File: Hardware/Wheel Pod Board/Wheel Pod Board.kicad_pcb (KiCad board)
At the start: 2 copper layers, 90 x 25.4 mm, 30 parts, among them J1 Conn_RJ-45, P1 UIM240XX_Stepper_Conn, P2 RS232, P3 ST_SWD_Connector, P4 SyRen, P5 BATT, U1 STM32F401RCT6, U2 SN75176BDR, U3 ZXCT1107, U4 ZXCT1107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

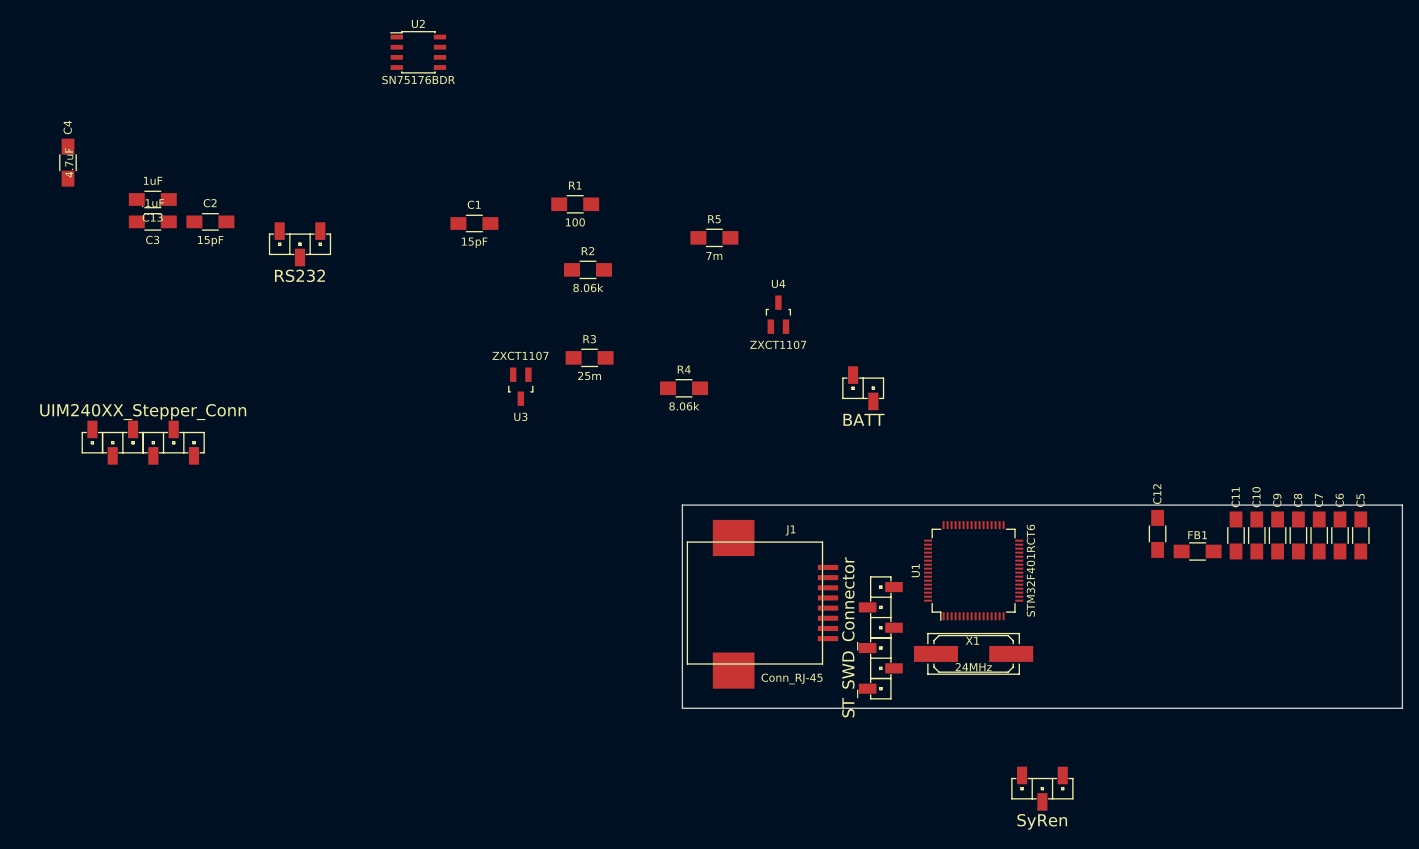
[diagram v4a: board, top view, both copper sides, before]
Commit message: Position components on PCB
Closes #4
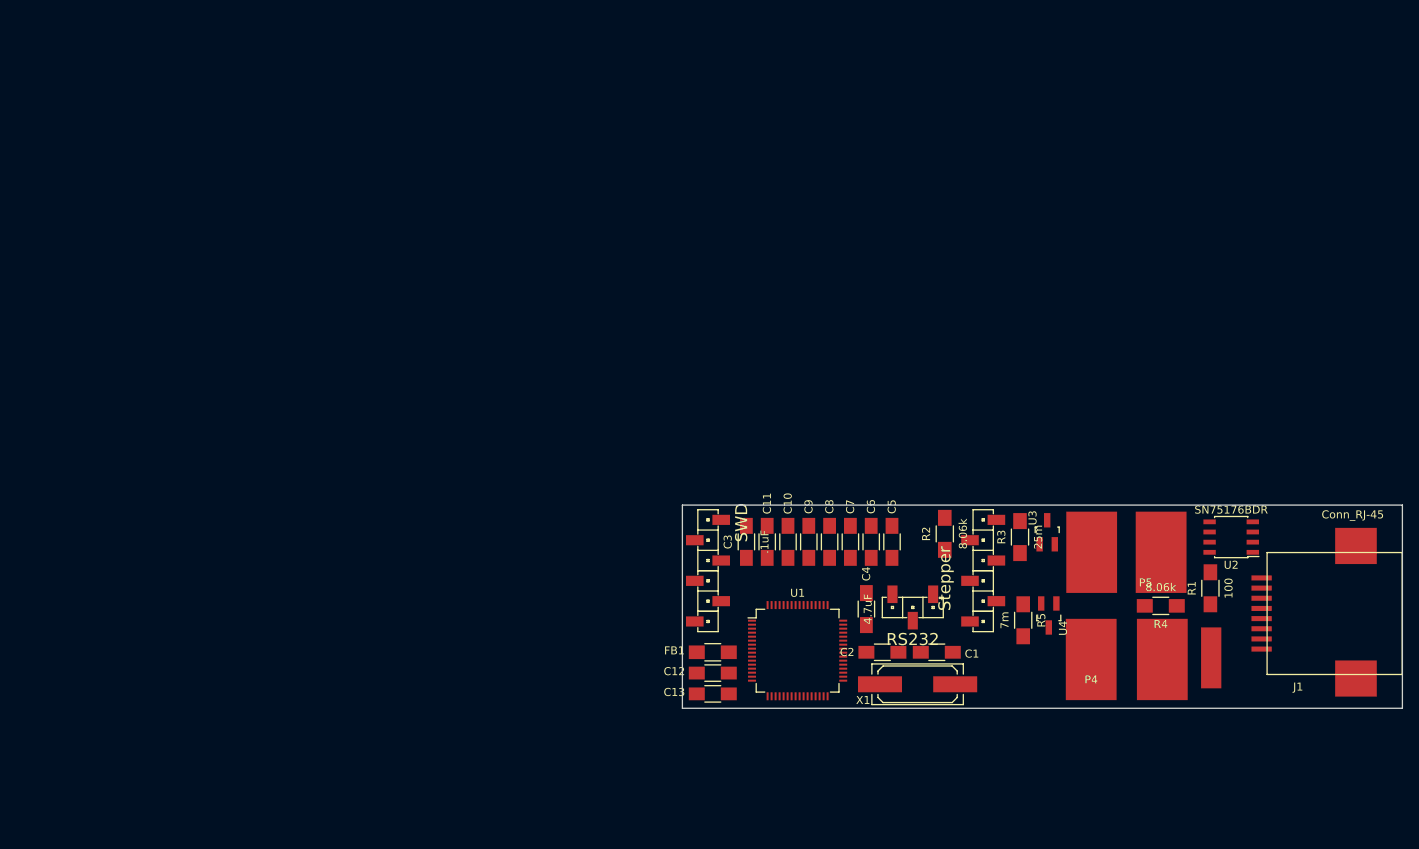
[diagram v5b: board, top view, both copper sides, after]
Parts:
- P1: value UIM240XX_Stepper_Conn -> Stepper
- P3: value ST_SWD_Connector -> SWD
- P4: footprint MAVRIC_footprints:1x3_SMD_header -> Wire_Pads:SolderWirePad_3x_0-8mmDrill
- P5: footprint MAVRIC_footprints:1x2_SMD_header -> Wire_Pads:SolderWirePad_2x_0-8mmDrill
- U3, U4: value ZXCT1107 -> (none)
- moved U2 118.3 mm to (262.0, 132.8), turned to 180 degrees
- moved C4 114.3 mm to (216.4, 141.8)
- moved P1 106.2 mm to (231.0, 137.0), turned to 270 degrees
- moved C2 99.8 mm to (218.4, 147.2)
- moved C13 93.4 mm to (197.2, 152.4)
- moved R1 92.8 mm to (259.4, 139.2), turned to 90 degrees
- moved P2 89.0 mm to (222.2, 141.6)
- moved C3 84.3 mm to (201.4, 133.4), turned to 90 degrees
- moved C1 78.8 mm to (225.2, 147.2), turned to 180 degrees
- moved U3 68.3 mm to (239.0, 132.2), turned to 0 degrees
- moved R4 65.5 mm to (253.2, 141.4), turned to 180 degrees
- moved FB1 61.9 mm to (197.2, 147.2), turned to 0 degrees
- moved R5 61.4 mm to (236.0, 143.2), turned to 270 degrees
- moved C11 58.6 mm to (204.0, 133.4)
- moved C6 58.6 mm to (217.0, 133.4)
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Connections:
- P1 pad 1: +12V -> /Stp+12V

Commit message: Begin routing PCB
Starting #8
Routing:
- net +3V3: track 0.00 -> 68.8 mm
- net GND: track 0.00 -> 44.0 mm, vias 0 -> 6
- net /VDDA: track 0.00 -> 5.73 mm
- added copper zone on B.Cu, net GND
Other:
- net class Default: clearance 0.254 -> 0.2032; trace_width 0.254 -> 0.2032
- rule trace_clearance: 0.254 -> 0.2032
- rule trace_min: 0.254 -> 0.2032
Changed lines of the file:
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@@
   (general
     (links 80)
-    (no_connects 80)
+    (no_connects 54)
     (area 193.349999 128.749999 283.450001 154.250001)
     (thickness 1.6)
     (drawings 4)
-    (tracks 0)
+    (tracks 52)
     (zones 0)
     (modules 30)
@@
   )
   (setup
-    (last_trace_width 0.254)
-    (trace_clearance 0.254)
-    (zone_clearance 0.508)
+    (last_trace_width 0.2032)
+    (user_trace_width 2.032)
+    (trace_clearance 0.2032)
+    (zone_clearance 0.1778)
     (zone_45_only no)
-    (trace_min 0.254)
+    (trace_min 0.2032)
     (segment_width 0.2)
     (edge_width 0.1)
@@
   (net 66 /USART2_TX)
   (net_class Default "This is the default net class."
-    (clearance 0.254)
-    (trace_width 0.254)
+    (clearance 0.2032)
+    (trace_width 0.2032)
     (via_dia 0.889)
     (via_drill 0.635)
@@
   (gr_line (start 193.4 154.2) (end 283.4 154.2) (angle 90) (layer Edge.Cuts) (width 0.1))
   (gr_line (start 193.4 128.8) (end 193.4 154.2) (angle 90) (layer Edge.Cuts) (width 0.1))
+  (segment (start 228.2 131.5) (end 228.2 132.04) (width 0.2032) (layer F.Cu) (net 40))
+  (via (at 228.2 131.5) (size 0.889) (layers F.Cu B.Cu) (net 40))
+  (segment (start 226.2 133.5) (end 228.2 131.5) (width 0.2032) (layer F.Cu) (net 40) (status 400000))
+  (segment (start 228.2 132.04) (end 229.35 133.19) (width 0.2032) (layer F.Cu) (net 40) (status 800000))
+  (segment (start 226.2 134.4) (end 226.2 133.5) (width 0.2032) (layer F.Cu) (net 40) (status C00000))
+  (segment (start 219.6 131.4) (end 220.8 131.4) (width 0.2032) (layer F.Cu) (net 40) (status 400000))
+  (via (at 221.5 130.7) (size 0.889) (layers F.Cu B.Cu) (net 40))
+  (segment (start 220.8 131.4) (end 221.5 130.7) (width 0.2032) (layer F.Cu) (net 40))
+  (segment (start 217 131.4) (end 219.6 131.4) (width 0.2032) (layer F.Cu) (net 40) (status C00000))
+  (segment (start 199.1 133) (end 199.8 133) (width 0.2032) (layer F.Cu) (net 40))
+  (segment (start 198.25 133.85) (end 199.1 133) (width 0.2032) (layer F.Cu) (net 40))
+  (via (at 199.1 133) (size 0.889) (layers F.Cu B.Cu) (net 40))
+  (segment (start 198.25 135.73) (end 198.25 133.85) (width 0.2032) (layer F.Cu) (net 40) (status 400000))
+  (segment (start 199.8 133) (end 201.4 131.4) (width 0.2032) (layer F.Cu) (net 40) (status 800000))
+  (segment (start 201.4 131.4) (end 206.6 131.4) (width 0.2032) (layer F.Cu) (net 40) (status C00000))
+  (segment (start 206.6 131.4) (end 209.2 131.4) (width 0.2032) (layer F.Cu) (net 40) (status C00000))
+  (segment (start 209.2 131.4) (end 211.8 131.4) (width 0.2032) (layer F.Cu) (net 40) (status C00000))
+  (segment (start 211.8 131.4) (end 214.4 131.4) (width 0.2032) (layer F.Cu) (net 40) (status C00000))
+  (segment (start 214.4 131.4) (end 217 131.4) (width 0.2032) (layer F.Cu) (net 40) (status C00000))
+  (segment (start 195.2 152.4) (end 195.2 149.8) (width 0.2032) (layer F.Cu) (net 40) (status C00000))
+  (segment (start 195.2 149.8) (end 195.6 149.4) (width 0.2032) (layer F.Cu) (net 40) (status C00000))
+  (segment (start 195.6 149.4) (end 197.1 149.4) (width 0.2032) (layer F.Cu) (net 40) (status 400000))
+  (via (at 197.1 149.4) (size 0.889) (layers F.Cu B.Cu) (net 40))
+  (segment (start 202.1 148.75) (end 203.15 148.75) (width 0.2032) (layer F.Cu) (net 40) (status 400000))
+  (segment (start 204.55 150.15) (end 204.55 152.7) (width 0.2032) (layer F.Cu) (net 40))
+  (via (at 204 149.6) (size 0.889) (layers F.Cu B.Cu) (net 40))
+  (segment (start 204.55 150.15) (end 204 149.6) (width 0.2032) (layer F.Cu) (net 40))
+  (segment (start 203.15 148.75) (end 204 149.6) (width 0.2032) (layer F.Cu) (net 40))
+  (segment (start 211.05 152.7) (end 211.05 151.65) (width 0.2032) (layer F.Cu) (net 40))
+  (via (at 210.8 151.4) (size 0.889) (layers F.Cu B.Cu) (net 40))
+  (segment (start 211.05 151.65) (end 210.8 151.4) (width 0.2032) (layer F.Cu) (net 40))
+  (segment (start 195.2 147.2) (end 196.4 147.2) (width 0.2032) (layer F.Cu) (net 44) (status 400000))
+  (segment (start 196.4 147.2) (end 204.05 139.55) (width 0.2032) (layer F.Cu) (net 44))
+  (segment (start 211.55 152.7) (end 211.55 144.35) (width 0.2032) (layer F.Cu) (net 44))
+  (segment (start 211.55 144.35) (end 210.45 143.25) (width 0.2032) (layer F.Cu) (net 44))
+  (segment (start 205.05 152.7) (end 205.05 145.05) (width 0.2032) (layer F.Cu) (net 44))
+  (segment (start 203.25 143.25) (end 202.1 143.25) (width 0.2032) (layer F.Cu) (net 44))
+  (segment (start 205.05 145.05) (end 203.25 143.25) (width 0.2032) (layer F.Cu) (net 44))
+  (segment (start 202.1 143.25) (end 210.45 143.25) (width 0.2032) (layer F.Cu) (net 44))
+  (segment (start 210.45 143.25) (end 213.5 143.25) (width 0.2032) (layer F.Cu) (net 44))
+  (segment (start 204.05 141.3) (end 202.1 143.25) (width 0.2032) (layer F.Cu) (net 44))
+  (segment (start 204.05 141.3) (end 204.05 139.55) (width 0.2032) (layer F.Cu) (net 44))
+  (segment (start 204.05 139.55) (end 204.05 135.45) (width 0.2032) (layer F.Cu) (net 44))
+  (segment (start 204.05 135.45) (end 204.1 135.4) (width 0.2032) (layer F.Cu) (net 44))
+  (segment (start 204.1 135.4) (end 209.2 135.4) (width 0.2032) (layer F.Cu) (net 44))
+  (segment (start 209.2 135.4) (end 211.8 135.4) (width 0.2032) (layer F.Cu) (net 44))
+  (segment (start 211.8 135.4) (end 214.4 135.4) (width 0.2032) (layer F.Cu) (net 44))
+  (segment (start 214.4 135.4) (end 217 135.4) (width 0.2032) (layer F.Cu) (net 44))
+  (segment (start 217 135.4) (end 219.6 135.4) (width 0.2032) (layer F.Cu) (net 44))
+  (segment (start 199.2 147.2) (end 199.2 149.8) (width 0.2032) (layer F.Cu) (net 45) (status C00000))
+  (segment (start 199.2 149.8) (end 199.75 149.25) (width 0.2032) (layer F.Cu) (net 45) (status C00000))
+  (segment (start 199.75 149.25) (end 202.1 149.25) (width 0.2032) (layer F.Cu) (net 45) (status C00000))
+  (zone (net 40) (net_name GND) (layer B.Cu) (hatch edge 0.508)
+    (connect_pads (clearance 0.1778))
+    (min_thickness 0.1778)
+    (fill yes (arc_segments 16) (thermal_gap 0.508) (thermal_bridge_width 0.508))
+    (polygon
+      (pts
+        (xy 283.2 154) (xy 193.6 154) (xy 193.6 129) (xy 283.2 129)
+      )
+    )
+  )
 )

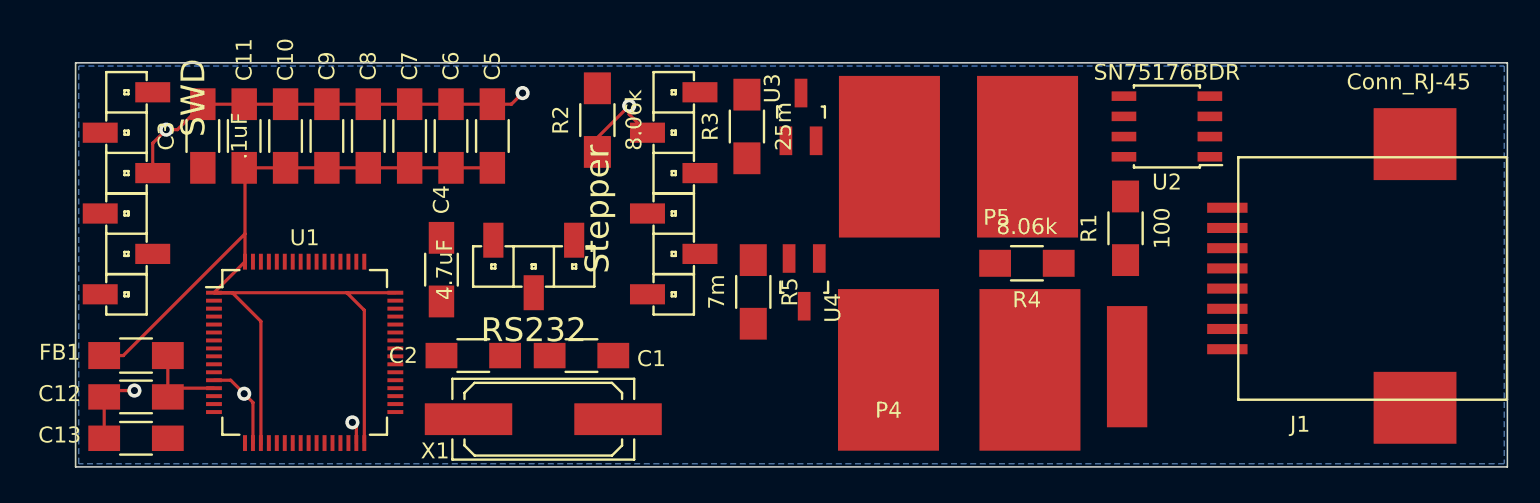
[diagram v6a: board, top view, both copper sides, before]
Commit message: Route all components, generate export + images
Progressing #8, Close #9 for now
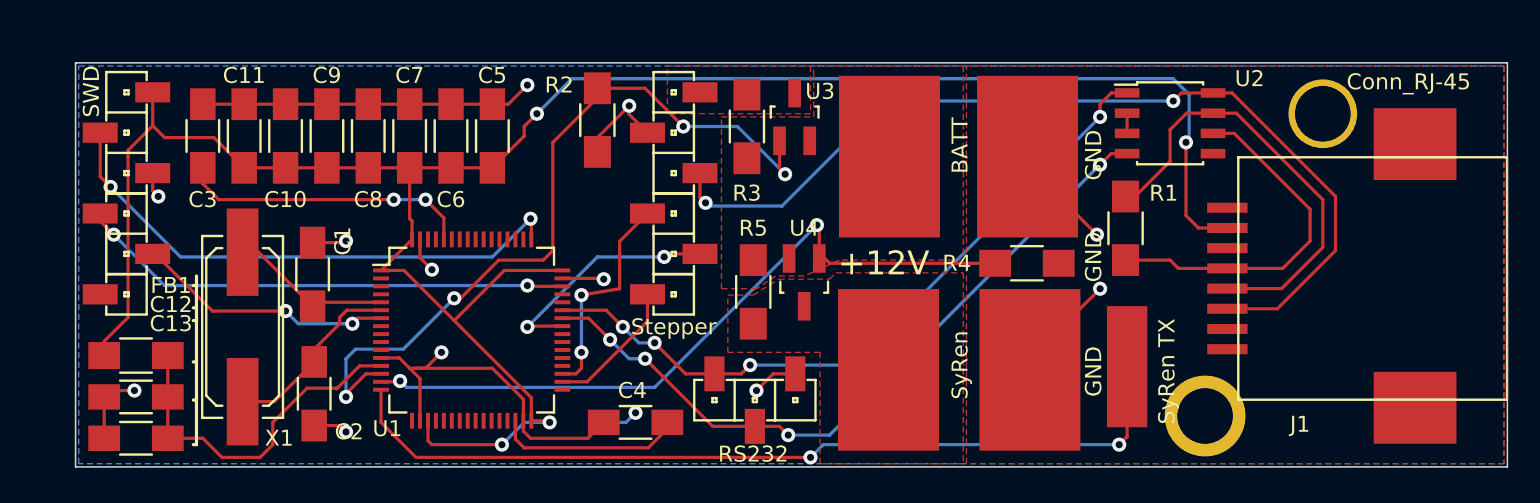
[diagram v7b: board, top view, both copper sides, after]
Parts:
- added MountingHole_3-5mm: VAL**, MAVRIC_footprints:PlatedMountingHole_3-5mm, F.Cu at (264.4, 151.0)
- added MountingHole_3-5mm: VAL**, MAVRIC_footprints:PlatedMountingHole_3-5mm, F.Cu at (271.8, 132.0)
- C4: value 4.7uF -> w4.7uF
- U2: value SN75176BDR -> (none)
- moved X1 19.8 mm to (203.9, 145.4), turned to 270 degrees
- moved C1 17.7 mm to (208.3, 142.1), turned to 90 degrees
- moved P2 16.2 mm to (236.1, 150.0)
- moved C4 15.5 mm to (228.6, 151.4), turned to 180 degrees
- moved U1 10.6 mm to (218.3, 145.6)
- moved C2 10.3 mm to (208.4, 149.6), turned to 270 degrees
- moved U3 0.40 mm to (238.6, 132.2)
- moved U2 0.28 mm to (262.2, 132.6), turned to 0 degrees
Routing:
- net +3V3: track 68.8 -> 138.2 mm, vias 0 -> 4
- net +5V: track 0.00 -> 59.1 mm, vias 0 -> 2
- net /USART2_TX: track 0.00 -> 54.8 mm, vias 0 -> 2
- net /StepperCurrent: track 0.00 -> 48.8 mm, vias 0 -> 4
- net /USART1_TX: track 0.00 -> 45.9 mm, vias 0 -> 4
- net /SyRenCurrent: track 0.00 -> 45.1 mm, vias 0 -> 2
- net /USART1_RX: track 0.00 -> 44.9 mm, vias 0 -> 4
- net GND: track 44.0 -> 86.5 mm, vias 6 -> 12
- net /SWCLK: track 0.00 -> 34.2 mm, vias 0 -> 2
- net /SWDIO: track 0.00 -> 31.2 mm, vias 0 -> 2
- net Net-(J1-Pad4): track 0.00 -> 28.1 mm
- net Net-(J1-Pad5): track 0.00 -> 22.6 mm
- net Net-(C3-Pad1): track 0.00 -> 18.4 mm, vias 0 -> 2
- net /VDDA: track 5.73 -> 23.1 mm
- net /NRST: track 0.00 -> 16.3 mm, vias 0 -> 2
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- added copper zone on F.Cu, net +12V
- added copper zone on F.Cu, net /Stp+12V
- added copper zone on F.Cu, net GND
- added copper zone on F.Cu, net Net-(P4-Pad2)
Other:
- board text added: "+12V"
- board text added: "GND"
- board text added: "SyRen TX"

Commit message: Progress on new pcb route
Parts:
- removed MountingHole_3-5mm (x2): VAL**, MAVRIC_footprints:PlatedMountingHole_3-5mm
- C4: value w4.7uF -> 4.7uF
- P1: value Stepper -> UIM240XX_Stepper_Conn; footprint MAVRIC_footprints:1x6_SMD_header -> MAVRIC_footprints:SolderWirePad_6xInline_0-8mmDrill
- P3: value SWD -> ST_SWD_Connector
- P4, P5, R3, R4, R5: moved to B.Cu
- U2: value (none) -> SN75176BDR
- U3, U4: value (none) -> ZXCT1107; moved to B.Cu
- moved P3 59.8 mm to (255.7, 146.1), turned to 90 degrees
- moved P1 38.3 mm to (266.4, 151.6), turned to 0 degrees
- moved U4 31.0 mm to (270.2, 141.6), turned to 90 degrees
- moved R5 30.0 mm to (265.9, 142.8)
- moved R3 27.3 mm to (262.7, 136.1), turned to 180 degrees
- moved C12 26.5 mm to (223.7, 149.8)
- moved C13 26.5 mm to (223.7, 152.4)
- moved FB1 26.5 mm to (223.7, 147.2)
- moved P5 26.4 mm to (277.7, 134.3)
- moved P4 26.2 mm to (270.7, 148.8)
- moved X1 26.1 mm to (229.9, 144.8)
- moved C1 25.9 mm to (234.2, 141.6)
- moved C2 25.8 mm to (234.2, 148.3)
- moved U1 25.7 mm to (243.9, 144.8)
- moved R2 25.5 mm to (241.4, 152.8), turned to 180 degrees
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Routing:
- net /USART2_TX: track 54.8 -> 0.00 mm, vias 2 -> 0
- net /SyRenCurrent: track 45.1 -> 0.00 mm, vias 2 -> 0
- net /StepperCurrent: track 48.8 -> 6.16 mm, vias 4 -> 0
- net +3V3: track 138.2 -> 101.0 mm, vias 4 -> 0
- net +5V: track 59.1 -> 29.4 mm, vias 2 -> 0
- net /USART1_TX: track 45.9 -> 24.6 mm, vias 4 -> 0
- net /SWDIO: track 31.2 -> 10.3 mm
- net /USART1_RX: track 44.9 -> 25.6 mm, vias 4 -> 0
- net /NRST: track 16.3 -> 0.00 mm, vias 2 -> 0
- net /SWCLK: track 34.2 -> 18.5 mm
- net /Step_Step: track 15.0 -> 0.00 mm, vias 2 -> 0
- net /Step_Direction: track 13.8 -> 0.00 mm, vias 2 -> 0
- net GND: track 86.5 -> 96.7 mm, vias 12 -> 7
- net /Step_Enable: track 8.62 -> 0.00 mm
- net Net-(C4-Pad1): track 11.8 -> 5.17 mm
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- added copper zone on B.Cu, net +12V
- added copper zone on B.Cu, net /Stp+12V
- added copper zone on B.Cu, net Net-(P4-Pad2)
- removed copper zone on F.Cu, net +12V
- removed copper zone on F.Cu, net /Stp+12V
- removed copper zone on F.Cu, net Net-(P4-Pad2)
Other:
- board size 90 x 25.4 mm -> 90 x 25.5 mm
